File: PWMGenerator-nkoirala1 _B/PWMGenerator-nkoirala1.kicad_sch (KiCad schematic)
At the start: 30 parts, among them J2 Conn_01x03_Pin, Q1 2N3904, Q2 2N3906, Q3 2N3904, Q4 2N3906, SW1 SW_SPST, U1 LM7805_TO220, U2 LM339

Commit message: commit
tryma fix etc run error
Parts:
- C1: value C_Polarized_US_220u -> 220uF
- C2: value C_Polarized -> 0.1uF
- C3: value C_Polarized_US_10u -> 10uF
- F2: value Polyfuse -> 0.5_AMP
- R1, R8: value R_US -> 2.2kΩ
- R10: value R_US -> 180Ω
- R2: value R_US -> 1MΩ
- R3: value R_US -> 330Ω
- R4: value R_US -> 10kΩ
- R5: value R_US -> 220kΩ
- R6: value R_US -> 390kΩ
- R7: value R_US -> 22kΩ
- R9: value R_US -> 8.2kΩ
- RV1: value R_Potentiometer -> 5kΩ
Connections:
- net VCC: no longer U2.5 (+)
- net at R8.2, RV1.1: now also U2.5 (+)
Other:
- moved on the sheet: C1, C2, C3, D2, D6, F2, Q1, Q2, R9, U2A, U2B

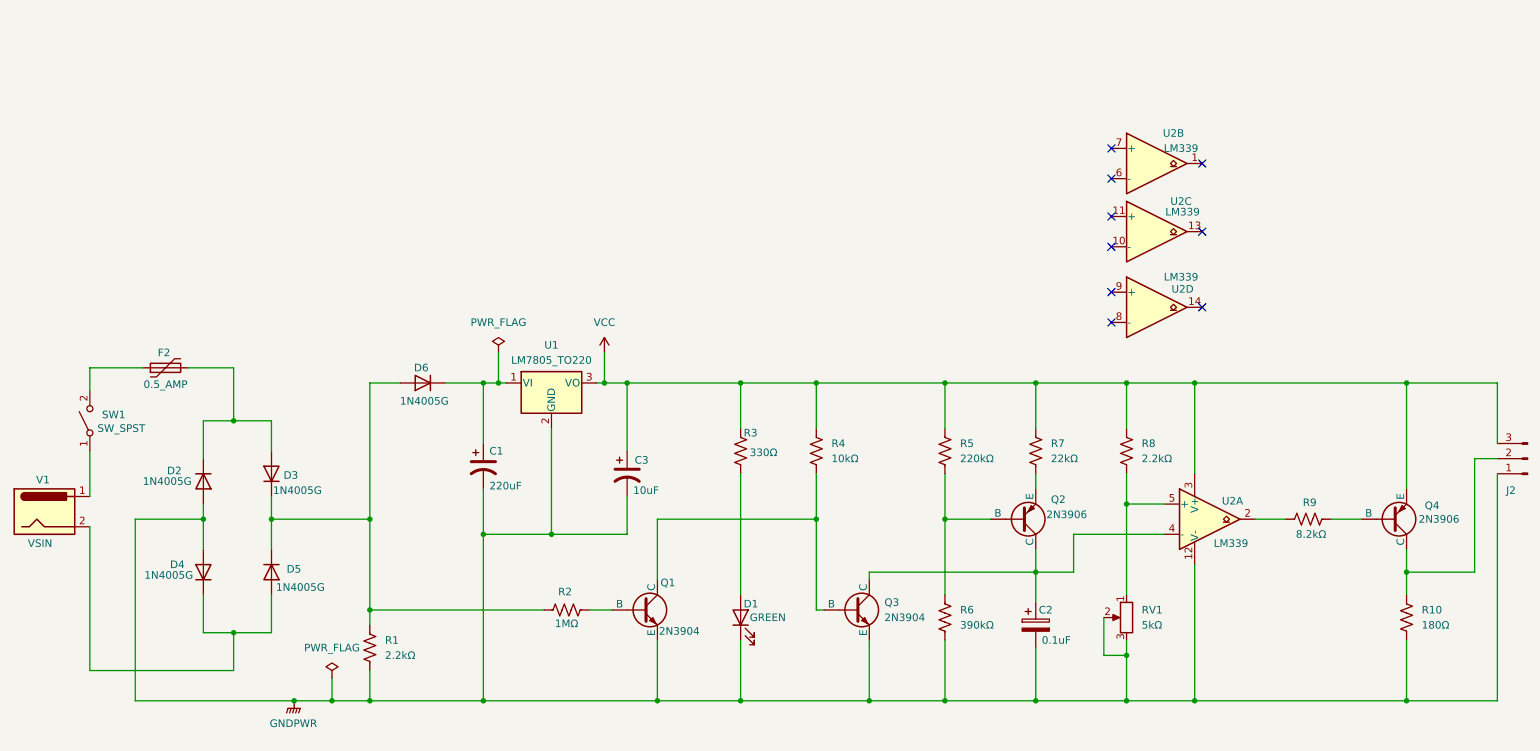
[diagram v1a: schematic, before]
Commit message: took a long time but its complete OArt B
had wrong npn
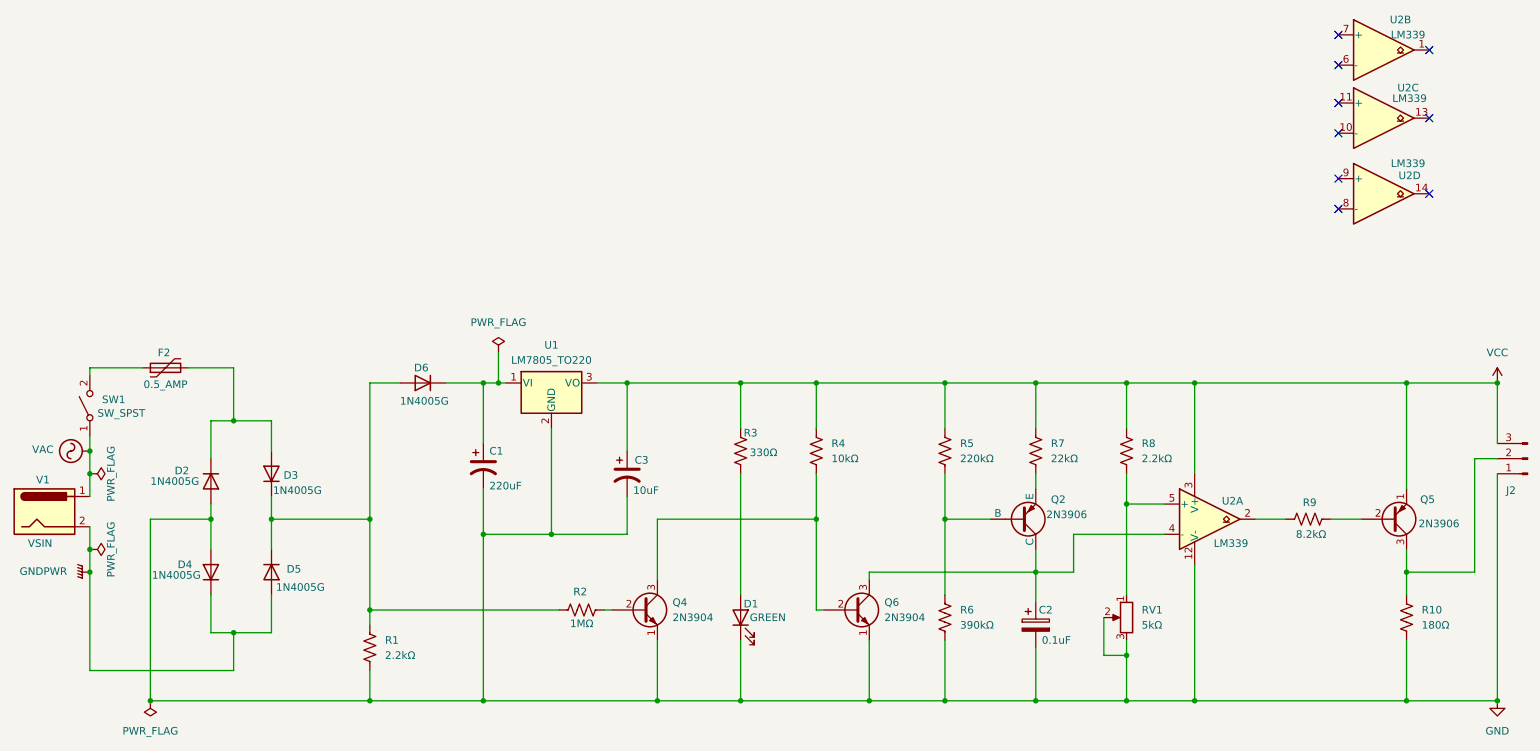
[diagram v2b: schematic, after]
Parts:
- removed Q1, Q3: 2N3904, Package_TO_SOT_SMD:SOT-23, symbol Simulation_SPICE:NPN
- removed Q4: 2N3906, Package_TO_SOT_SMD:SOT-23, symbol Simulation_SPICE:PNP
- added Q4, Q6: 2N3904, Package_TO_SOT_SMD:SOT-23, symbol Transistor_BJT:2N3904
- added Q5: 2N3906, Package_TO_SOT_SMD:SOT-23, symbol Transistor_BJT:2N3906
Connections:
- net GNDPWR: now also D4.1 (K), D5.2 (A), V1.2; no longer C1.2, C2.2, C3.2, D1.1 (K), D2.2 (A), D4.2 (A), J2.1 (Pin_1), R1.2, R10.2, R6.2, RV1.2, RV1.3, U1.2 (GND), U2.12 (V-)
- net VCC: now also Q5.1 (E)
- net VAC: now reaches SW1.1 (A), V1.1
- net at C2.1, Q2.1 (C), U2.4 (-): now also Q6.3 (C)
- net at R4.2: now also Q4.3 (C), Q6.2 (B)
- net at R2.2: now also Q4.2 (B)
- net at R9.2: now also Q5.2 (B)
- net at J2.2 (Pin_2), R10.1: now also Q5.3 (C)
- new net GND: C1.2, C2.2, C3.2, D1.1 (K), D2.2 (A), D4.2 (A), J2.1 (Pin_1), Q4.1 (E), Q6.1 (E), R1.2, R10.2, R6.2, RV1.2, RV1.3, U1.2 (GND), U2.12 (V-)
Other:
- moved on the sheet: D2, D4, R2, SW1, U2B, U2C, U2D
